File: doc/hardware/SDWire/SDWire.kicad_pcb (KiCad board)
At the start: 4 copper layers, 21.6 x 48.4 mm, 83 parts, among them J1 usd-plug, J2 uSD Socket, P1 USB_OTG_MICRO_USB, Q3 MMBT4403LT1, Q4 MMBT4403LT1, U1 USB2640-HZH-02, U2 SPX3819M5, U3 FT200XD, U4 MC74HC1G04DTT1G, U5 TS3A27518EPWR, U6 AT24CS02-SSHM, Y1 24MHz

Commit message: Change analog switch to max4996
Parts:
- removed C22, C23: 47pF, Capacitors_SMD:C_0402
- removed R6, R7: 27R, Resistors_SMD:R_0402
- D6: value BLUE -> OSB50402C1E
- U5: value TS3A27518EPWR -> MAX4996L; footprint mux-footprints:TSSOP-24 -> SDWire:QFN40P350X350X80-25N
- moved U5 0.95 mm to (151.1, 110.6), turned to 180 degrees
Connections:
- U3 pad 1: Net-(R6-Pad1) -> /USB_B-
- U3 pad 10: Net-(R7-Pad1) -> /USB_B+
- U5 pad 1: /DAT3_DUT -> /SOCKET_SEL
- U5 pad 10: Net-(J2-Pad3) -> /DAT0_DUT
- U5 pad 11: /DAT2_TS -> /DAT3_DUT
- U5 pad 12: Net-(J2-Pad8) -> /DAT2_DUT
- U5 pad 13: /DAT3_TS -> GND
- U5 pad 14: /SOCKET_SEL -> +3V3
- U5 pad 15: /DAT0_TS -> GND
- U5 pad 16: /DAT1_TS -> Net-(J2-Pad7)
- U5 pad 17: /CLK_TS -> Net-(J2-Pad2)
- U5 pad 18: /CMD_TS -> Net-(J2-Pad1)
- U5 pad 19: /CMD_DUT -> /DAT2_TS
- U5 pad 2: /DAT2_DUT -> /SOCKET_SEL
- U5 pad 20: GND -> /DAT3_TS
- U5 pad 21: /CLK_DUT -> /DAT0_TS
- U5 pad 22: /DAT1_DUT -> /CLK_TS
- U5 pad 23: /DAT0_DUT -> /CMD_TS
- U5 pad 24: /SOCKET_SEL -> /DAT1_TS
- U5 pad 3: Net-(U5-Pad3) -> /SOCKET_SEL
- U5 pad 4: Net-(J2-Pad1) -> Net-(J2-Pad5)
- U5 pad 5: GND -> Net-(J2-Pad3)
- U5 pad 6: Net-(J2-Pad2) -> Net-(J2-Pad8)
- U5 pad 7: Net-(J2-Pad7) -> /DAT1_DUT
- U5 pad 8: +3V3 -> /CMD_DUT
- U5 pad 9: Net-(J2-Pad5) -> /CLK_DUT
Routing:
- net /SOCKET_SEL: track 77.6 -> 67.4 mm, vias 5 -> 3
- net Net-(J2-Pad8): track 7.42 -> 17.2 mm
- net /DAT2_TS: track 11.0 -> 3.69 mm
- net /DAT3_TS: track 10.8 -> 3.65 mm, vias 2 -> 0
- net /CMD_TS: track 11.0 -> 5.28 mm, vias 0 -> 2
- net Net-(J2-Pad3): track 7.42 -> 12.7 mm
- net Net-(J2-Pad5): track 10.00 -> 14.5 mm
- net Net-(J2-Pad1): track 5.44 -> 9.52 mm
- net Net-(J2-Pad2): track 4.84 -> 8.19 mm
- net Net-(R7-Pad1): track 1.76 -> 0.00 mm
- net Net-(R6-Pad1): track 1.68 -> 0.00 mm
- net GND: track 114.8 -> 116.2 mm, vias 14 -> 13
- net /CLK_TS: track 10.7 -> 9.33 mm, vias 0 -> 2
- net Net-(J2-Pad7): track 7.26 -> 8.56 mm
- net /USB_B-: track 11.2 -> 12.1 mm
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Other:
- board text added: "SDWire v2.0"
- board text removed: "SDWire v1.4"

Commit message: Update solder paste and solder mask layers
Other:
- rule pad_to_mask_clearance: 0.13 -> 0.05

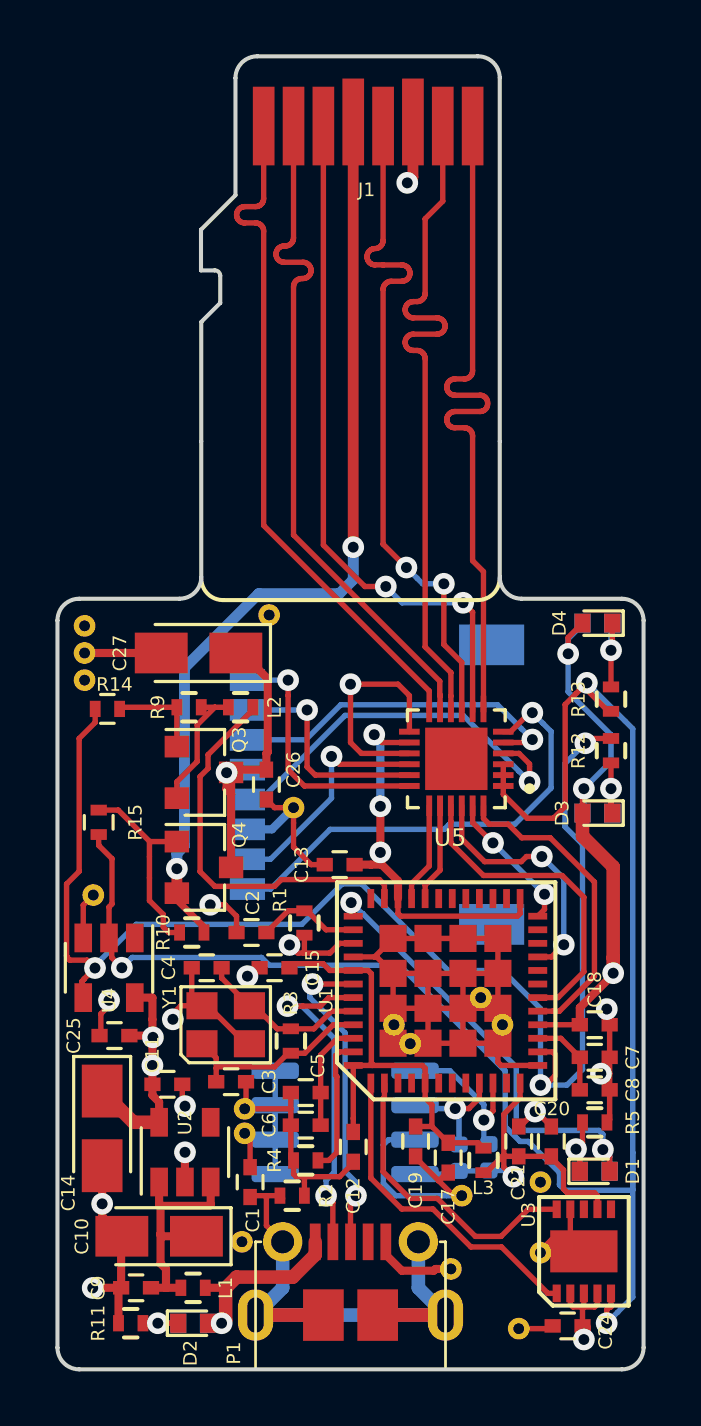
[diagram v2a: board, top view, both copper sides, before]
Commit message: Change uSD connector due to availabilty problems
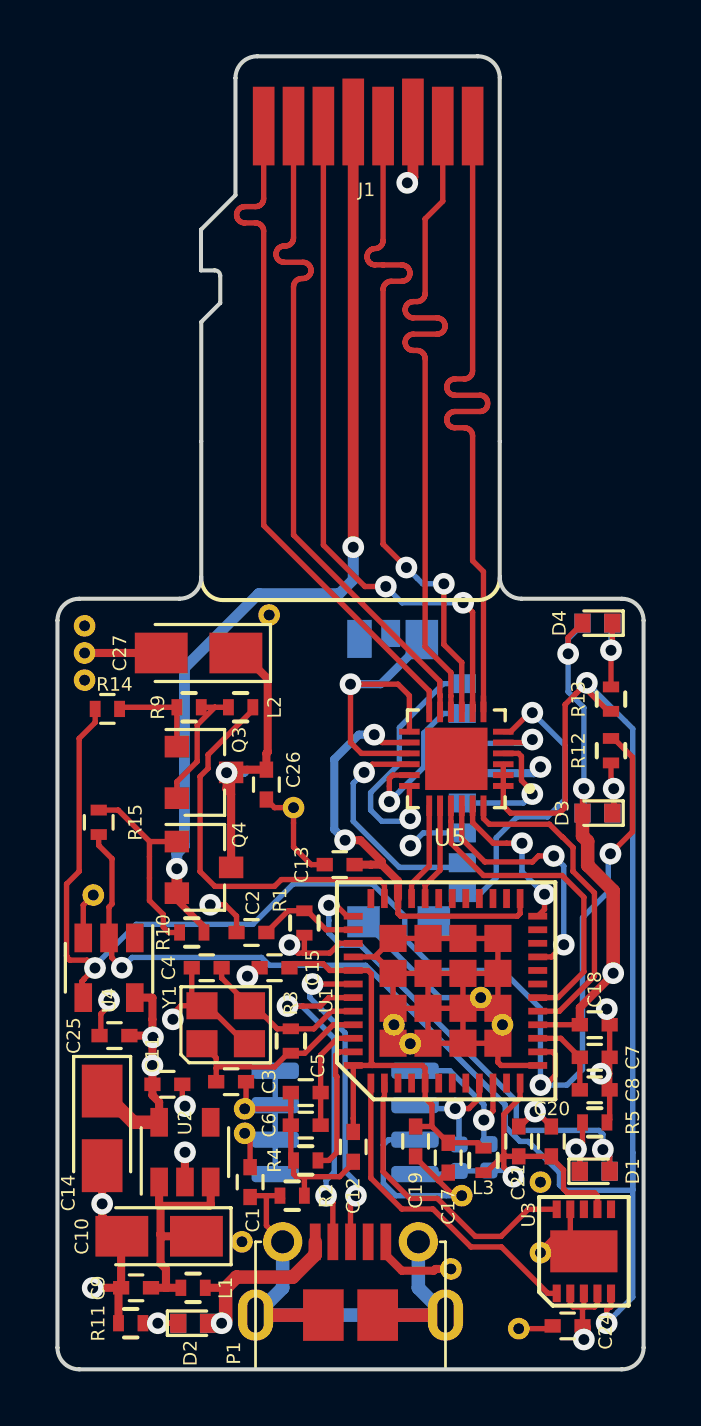
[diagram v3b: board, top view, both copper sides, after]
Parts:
- J2: value uSD Socket -> 47571-0001; footprint mux-footprints:usd-attend -> SDWire:475710001
- moved J2 7.45 mm to (149.9, 111.4)
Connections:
- U5 pad 16: Net-(J2-Pad7) -> Net-(J2-PadP7)
- U5 pad 17: Net-(J2-Pad2) -> Net-(J2-PadP2)
- U5 pad 18: Net-(J2-Pad1) -> Net-(J2-PadP1)
- U5 pad 4: Net-(J2-Pad5) -> Net-(J2-PadP5)
- U5 pad 5: Net-(J2-Pad3) -> Net-(J2-PadP3)
- U5 pad 6: Net-(J2-Pad8) -> Net-(J2-PadP8)
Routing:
- net Net-(J2-Pad8): track 17.2 -> 0.00 mm, vias 1 -> 0
- net /USD_VDD: track 11.5 -> 27.7 mm, vias 1 -> 2
- net Net-(J2-Pad5): track 14.5 -> 0.00 mm, vias 1 -> 0
- net Net-(J2-Pad3): track 12.7 -> 0.00 mm, vias 1 -> 0
- net Net-(J2-PadP8): track 0.00 -> 11.1 mm, vias 0 -> 1
- net Net-(J2-Pad1): track 9.52 -> 0.00 mm, vias 1 -> 0
- net Net-(J2-PadP1): track 0.00 -> 9.35 mm, vias 0 -> 1
- net GND: track 116.2 -> 125.1 mm, vias 13 -> 14
- net Net-(J2-Pad7): track 8.56 -> 0.00 mm, vias 1 -> 0
- net Net-(J2-PadP7): track 0.00 -> 8.55 mm, vias 0 -> 1
- net Net-(J2-Pad2): track 8.19 -> 0.00 mm, vias 1 -> 0
- net Net-(J2-PadP2): track 0.00 -> 6.41 mm, vias 0 -> 1
- net Net-(J2-PadP5): track 0.00 -> 4.99 mm, vias 0 -> 1
- net Net-(J2-PadP3): track 0.00 -> 3.76 mm, vias 0 -> 1
- net Net-(D1-Pad2): track 16.9 -> 18.1 mm
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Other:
- net class Default removed
- board text added: "SDWire v2.1"
- board text removed: "SDWire v2.0"
